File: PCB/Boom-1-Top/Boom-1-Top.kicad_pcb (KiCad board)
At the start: 4 copper layers, 345 x 165 mm, 770 parts, among them J1 DEBUG, J10 PIC_DEBUG, J11 PIC_DEBUG, J12 PIC_DEBUG, J13 PIC_DEBUG, J14 PIC_DEBUG, J15 USB_B_Micro, J16 SD_Card, J17 BT_DEBUG, J18 12V Supply, J19 3V3 Bypass, J2 MIDI IN, J20 5V Bypass, J3 MIDI OUT, J37 Osc1Conn, J38 Osc2Conn, J39 SubNoiseConn, J4 PIC_DEBUG, J40 FiltConn2, J41 EnvGenConn2, J42 EnvGenConn1, J43 FXConn1, J44 FiltConn1, J45 FXConn2, J46 EnvGenConn3, J5 PIC_DEBUG, J6 PIC_DEBUG, J7 PIC_DEBUG, J8 PIC_DEBUG, J9 PIC_DEBUG, Q1 AO3401A, Q2 AO3401A, SW1 Osc1SawEncoder, SW10 SubToOsc2FiltEncoder, SW11 Osc1ToOsc2FiltEncoder, SW12 Osc1FiltFreqEncoder, SW13 Osc2FiltFreqEncoder, SW14 SubFiltFreqEncoder, SW15 OscFiltEnvAttackEncoder, SW16 SubFiltEnvAttackEncoder, SW17 Osc1FiltResEncoder, SW18 Osc2FiltResEncoder, SW19 SubFiltResEncoder, SW2 Osc1SqrEncoder, SW20 OscFiltEnvDecayEncoder, SW21 SubFiltEnvDecayEncoder, SW22 OscFiltEnvSustainEncoder, SW23 SubFiltEnvSustainEncoder, SW24 Osc1DriveEncoder, SW25 Osc2DistortionEncoder, SW26 OscFiltEnvReleaseEncoder, SW27 SubFiltEnvReleaseEncoder, SW28 FXWetDryEncoder, SW29 SubAmpEnvAttackEncoder, SW3 Rotary_Encoder, SW30 OscAmpEnvAttackEncoder, SW31 FXControl1Encoder, SW32 SubAmpEnvDecayEncoder, SW33 OscAmpEnvDecayEncoder, SW34 FXControl2Encoder, SW35 SubAmpEnvSustainEncoder, SW36 OscAmpEnvSustainEncoder, SW37 FXControl3Encoder, SW38 FXFeedbackEncoder, SW39 SubAmpEnvReleaseEncoder, SW4 Rotary_Encoder_Switch, SW40 OscAmpEnvReleaseEncoder, SW41 Reset, SW43 Reset, SW5 Rotary_Encoder, SW53 Osc1TuneEncoder, SW6 SubToSubFiltEncoder, SW7 SubNoiseEncoder, U1 STM32F407VGTx, U10 DAC7678xPW, U11 PIC18F26Q43, U12 PIC18F26Q43, U13 PIC18F26Q43, U14 PIC18F26Q43, U15 PIC18F26Q43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

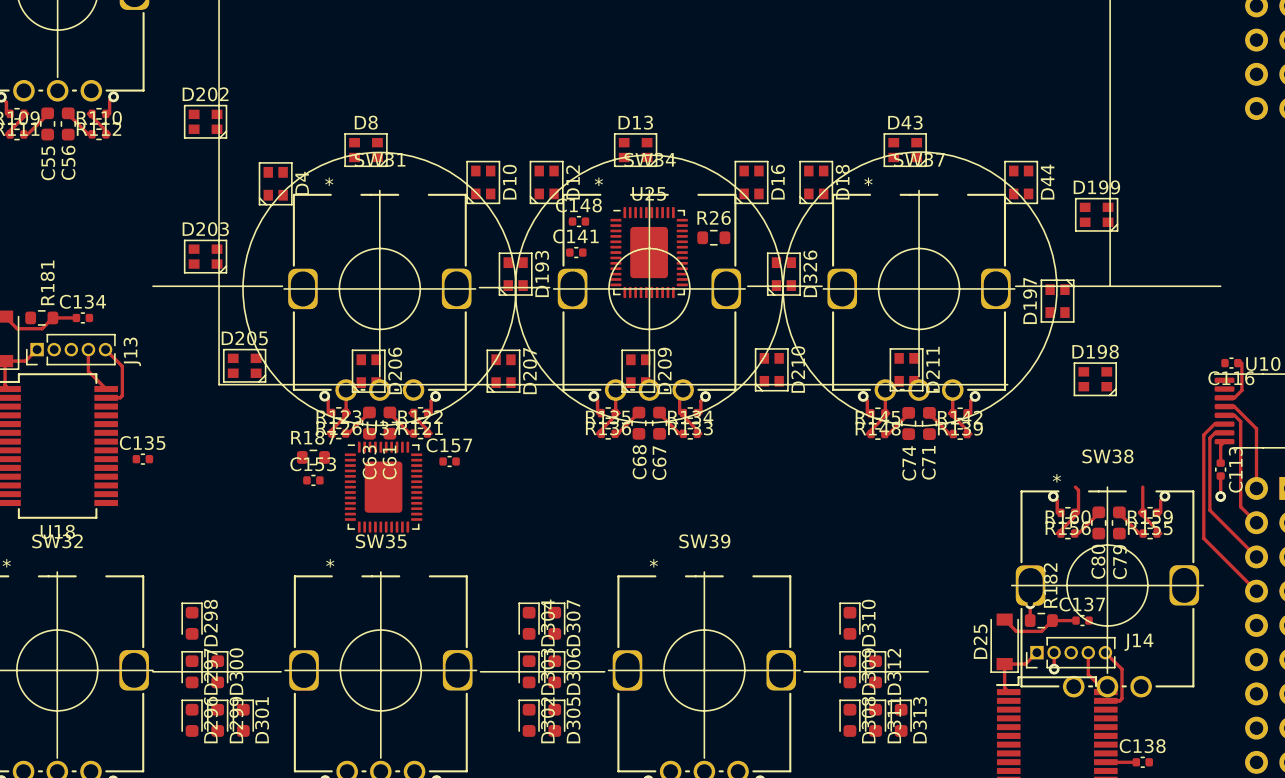
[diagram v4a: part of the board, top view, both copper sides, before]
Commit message: FX knobs in a row including feedback
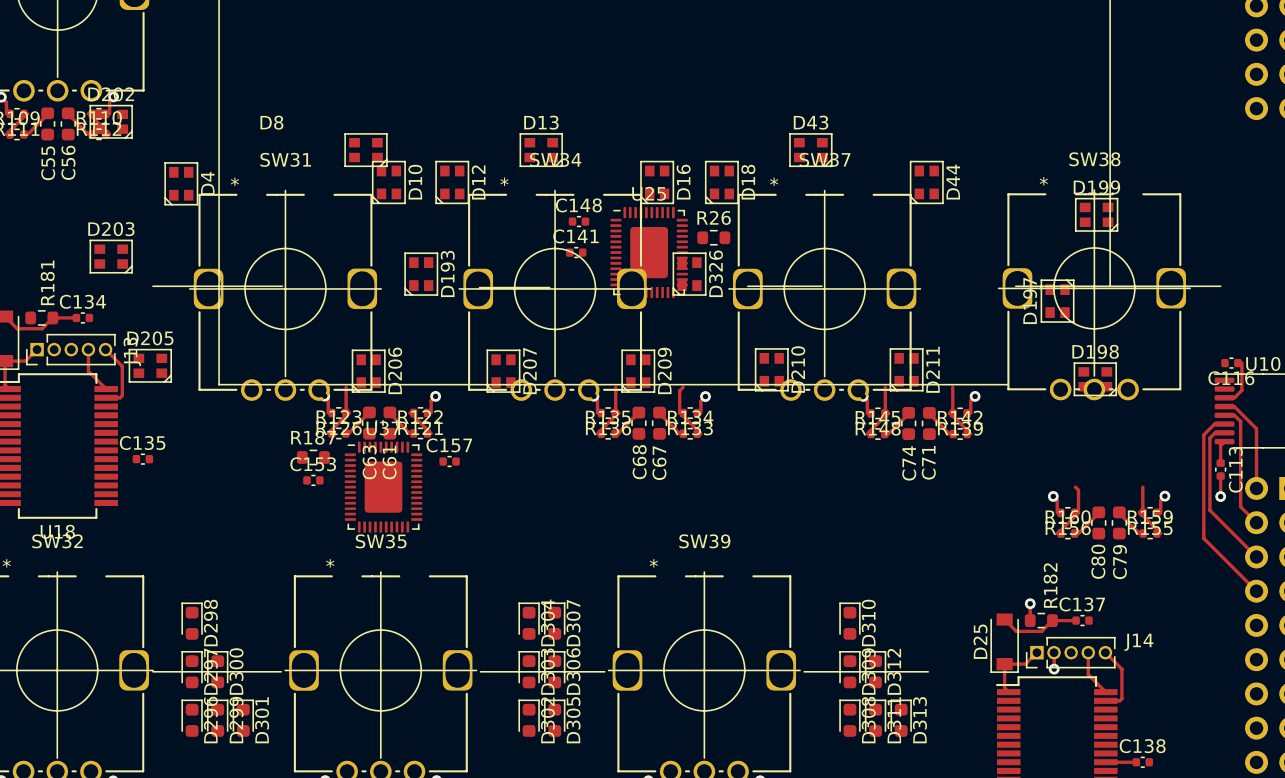
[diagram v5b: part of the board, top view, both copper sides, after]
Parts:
- moved SW38 22.1 mm to (454.9, 202.4)
- moved D10 7.00 mm to (405.1, 201.5)
- moved D12 7.00 mm to (409.8, 201.5)
- moved D13 7.00 mm to (416.4, 199.1)
- moved D16 7.00 mm to (425.0, 201.5)
- moved D18 7.00 mm to (429.8, 201.5)
- moved D193 7.00 mm to (407.5, 208.3)
- moved D202 7.00 mm to (384.5, 197.0)
- moved D203 7.00 mm to (384.5, 207.0)
- moved D205 7.00 mm to (387.4, 215.1)
- moved D326 7.00 mm to (427.4, 208.3)
- moved D4 7.00 mm to (389.7, 201.6)
- moved D43 7.00 mm to (436.4, 199.1)
- moved D44 7.00 mm to (445.0, 201.5)
- moved SW31 7.00 mm to (394.9, 202.4)
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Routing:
- net +5V: track 129.7 -> 125.6 mm, vias 81 -> 78
- net Net-(R139-Pad2): track 4.24 -> 5.62 mm, vias 0 -> 1
- net Net-(R133-Pad2): track 4.23 -> 5.59 mm, vias 0 -> 1
- net Net-(R121-Pad2): track 2.20 -> 3.56 mm, vias 0 -> 1
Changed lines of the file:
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@@
   (general
     (thickness 1.6)
-    (drawings 93)
+    (drawings 90)
     (tracks 1239)
     (zones 0)
@@
   )
   (module PEC11R:PEC11R-4x15F-N0024 locked (layer F.Cu)
-    (at 455.9 224.4)
+    (at 454.93 202.36)
     (fp_text reference SW38 (at 2.54 -2.54) (layer F.SilkS)
       (effects (font (size 1 1) (thickness 0.15)))
@@
   )
   (module PEC11R:PEC11R-4x15F-N0024 locked (layer F.Cu)
-    (at 441.925 202.4)
+    (at 434.925 202.4)
     (fp_text reference SW37 (at 2.54 -2.54) (layer F.SilkS)
       (effects (font (size 1 1) (thickness 0.15)))
@@
   )
   (module PEC11R:PEC11R-4x15F-N0024 locked (layer F.Cu)
-    (at 421.925 202.4)
+    (at 414.925 202.4)
     (fp_text reference SW34 (at 2.54 -2.54) (layer F.SilkS)
       (effects (font (size 1 1) (thickness 0.15)))
@@
   )
   (module PEC11R:PEC11R-4x15F-N0024 locked (layer F.Cu)
-    (at 401.925 202.4)
+    (at 394.925 202.4)
     (fp_text reference SW31 (at 2.54 -2.54) (layer F.SilkS)
       (effects (font (size 1 1) (thickness 0.15)))
@@
   )
   (module fm-b2020rgba-hg:FM-B2020RGBA-HG (layer F.Cu)
-    (at 434.4 208.3 270)
+    (at 427.4 208.3 270)
     (attr smd)
     (fp_text reference D326 (at 0 -2 90) (layer F.SilkS)
@@
   )
   (module fm-b2020rgba-hg:FM-B2020RGBA-HG (layer F.Cu)
-    (at 394.4 215.1)
+    (at 387.4 215.1)
     (attr smd)
     (fp_text reference D205 (at 0 -2) (layer F.SilkS)
@@
   )
   (module fm-b2020rgba-hg:FM-B2020RGBA-HG (layer F.Cu)
-    (at 391.5 207)
+    (at 384.5 207)
     (attr smd)
     (fp_text reference D203 (at 0 -2) (layer F.SilkS)
@@
   )
   (module fm-b2020rgba-hg:FM-B2020RGBA-HG (layer F.Cu)
-    (at 391.5 197)
+    (at 384.5 197)
     (attr smd)
     (fp_text reference D202 (at 0 -2) (layer F.SilkS)
@@
   )
   (module fm-b2020rgba-hg:FM-B2020RGBA-HG (layer F.Cu)
-    (at 414.5 208.3 270)
+    (at 407.5 208.3 270)
     (attr smd)
     (fp_text reference D193 (at 0 -2 90) (layer F.SilkS)
@@
   )
   (module fm-b2020rgba-hg:FM-B2020RGBA-HG (layer F.Cu)
-    (at 452 201.5 270)
+    (at 445 201.5 270)
     (attr smd)
     (fp_text reference D44 (at 0 -2 90) (layer F.SilkS)
@@
   )
   (module fm-b2020rgba-hg:FM-B2020RGBA-HG (layer F.Cu)
-    (at 443.4 199.1)
+    (at 436.4 199.1)
     (attr smd)
     (fp_text reference D43 (at 0 -2) (layer F.SilkS)
@@
   )
   (module fm-b2020rgba-hg:FM-B2020RGBA-HG (layer F.Cu)
-    (at 436.8 201.5 270)
+    (at 429.8 201.5 270)
     (attr smd)
     (fp_text reference D18 (at 0 -2 90) (layer F.SilkS)
@@
   )
   (module fm-b2020rgba-hg:FM-B2020RGBA-HG (layer F.Cu)
-    (at 432 201.5 270)
+    (at 425 201.5 270)
     (attr smd)
     (fp_text reference D16 (at 0 -2 90) (layer F.SilkS)
@@
   )
   (module fm-b2020rgba-hg:FM-B2020RGBA-HG (layer F.Cu)
-    (at 423.4 199.1)
+    (at 416.4 199.1)
     (attr smd)
     (fp_text reference D13 (at 0 -2) (layer F.SilkS)
@@
   )
   (module fm-b2020rgba-hg:FM-B2020RGBA-HG (layer F.Cu)
-    (at 416.8 201.5 270)
+    (at 409.8 201.5 270)
     (attr smd)
     (fp_text reference D12 (at 0 -2 90) (layer F.SilkS)
@@
   )
   (module fm-b2020rgba-hg:FM-B2020RGBA-HG (layer F.Cu)
-    (at 412.1 201.5 270)
+    (at 405.1 201.5 270)
     (attr smd)
     (fp_text reference D10 (at 0 -2 90) (layer F.SilkS)
@@
     (at 403.4 199.1)
     (attr smd)
-    (fp_text reference D8 (at 0 -2) (layer F.SilkS)
+    (fp_text reference D8 (at -7 -2) (layer F.SilkS)
       (effects (font (size 1 1) (thickness 0.15)))
     )
@@
   )
   (module fm-b2020rgba-hg:FM-B2020RGBA-HG (layer F.Cu)
-    (at 396.7 201.6 270)
+    (at 389.7 201.6 270)
     (attr smd)
     (fp_text reference D4 (at 0 -2 90) (layer F.SilkS)
@@
     (arrow2b (pts (xy 160.7 114.2) (xy 161.286421 115.326504)))
   )
-  (gr_circle (center 444.5 209.4) (end 436.7 202.9) (layer F.SilkS) (width 0.12))
-  (gr_circle (center 424.4 209.4) (end 416.9 202.9) (layer F.SilkS) (width 0.12))
-  (gr_circle (center 404.4 209.4) (end 411.2 201.9) (layer F.SilkS) (width 0.12))
   (gr_line (start 435.9 237.8) (end 445.1 237.8) (layer F.SilkS) (width 0.12))
   (gr_line (start 327.8 156.8) (end 336.9 156.8) (layer F.SilkS) (width 0.12))
@@
   (segment (start 432.3175 246.2025) (end 432.64 245.88) (width 0.25) (layer F.Cu) (net 204))
   (segment (start 432.3175 247.12) (end 432.3175 246.2025) (width 0.25) (layer F.Cu) (net 204))
-  (via (at 400.335 217.35) (size 0.8) (drill 0.4) (layers F.Cu B.Cu) (net 204))
-  (segment (start 400.595 217.61) (end 400.335 217.35) (width 0.25) (layer F.Cu) (net 204))
-  (segment (start 400.595 218.6) (end 400.595 217.61) (width 0.25) (layer F.Cu) (net 204))
+  (via (at 400.335 217.35) (size 0.8) (drill 0.4) (layers F.Cu B.Cu) (net 247))
+  (segment (start 400.595 217.61) (end 400.335 217.35) (width 0.25) (layer F.Cu) (net 247))
+  (segment (start 400.595 218.6) (end 400.595 217.61) (width 0.25) (layer F.Cu) (net 247))
   (via (at 408.565 217.37) (size 0.8) (drill 0.4) (layers F.Cu B.Cu) (net 204))
   (segment (start 408.2325 217.7025) (end 408.565 217.37) (width 0.25) (layer F.Cu) (net 204))
   (segment (start 408.2325 218.6) (end 408.2325 217.7025) (width 0.25) (layer F.Cu) (net 204))
-  (segment (start 420.5775 217.6325) (end 420.305 217.36) (width 0.25) (layer F.Cu) (net 204))
-  (via (at 420.305 217.36) (size 0.8) (drill 0.4) (layers F.Cu B.Cu) (net 204))
-  (segment (start 420.5775 218.61) (end 420.5775 217.6325) (width 0.25) (layer F.Cu) (net 204))
+  (segment (start 420.5775 217.6325) (end 420.305 217.36) (width 0.25) (layer F.Cu) (net 253))
+  (via (at 420.305 217.36) (size 0.8) (drill 0.4) (layers F.Cu B.Cu) (net 253))
+  (segment (start 420.5775 218.61) (end 420.5775 217.6325) (width 0.25) (layer F.Cu) (net 253))
   (via (at 428.585 217.38) (size 0.8) (drill 0.4) (layers F.Cu B.Cu) (net 204))
   (segment (start 428.2425 217.7225) (end 428.585 217.38) (width 0.25) (layer F.Cu) (net 204))
   (segment (start 428.2425 218.61) (end 428.2425 217.7225) (width 0.25) (layer F.Cu) (net 204))
-  (via (at 440.285 217.37) (size 0.8) (drill 0.4) (layers F.Cu B.Cu) (net 204))
-  (segment (start 440.5875 217.6725) (end 440.285 217.37) (width 0.25) (layer F.Cu) (net 204))
-  (segment (start 440.5875 218.63) (end 440.5875 217.6725) (width 0.25) (layer F.Cu) (net 204))
+  (via (at 440.285 217.37) (size 0.8) (drill 0.4) (layers F.Cu B.Cu) (net 257))
+  (segment (start 440.5875 217.6725) (end 440.285 217.37) (width 0.25) (layer F.Cu) (net 257))
+  (segment (start 440.5875 218.63) (end 440.5875 217.6725) (width 0.25) (layer F.Cu) (net 257))
   (segment (start 448.2625 217.6925) (end 448.585 217.37) (width 0.25) (layer F.Cu) (net 204))
   (via (at 448.585 217.37) (size 0.8) (drill 0.4) (layers F.Cu B.Cu) (net 204))

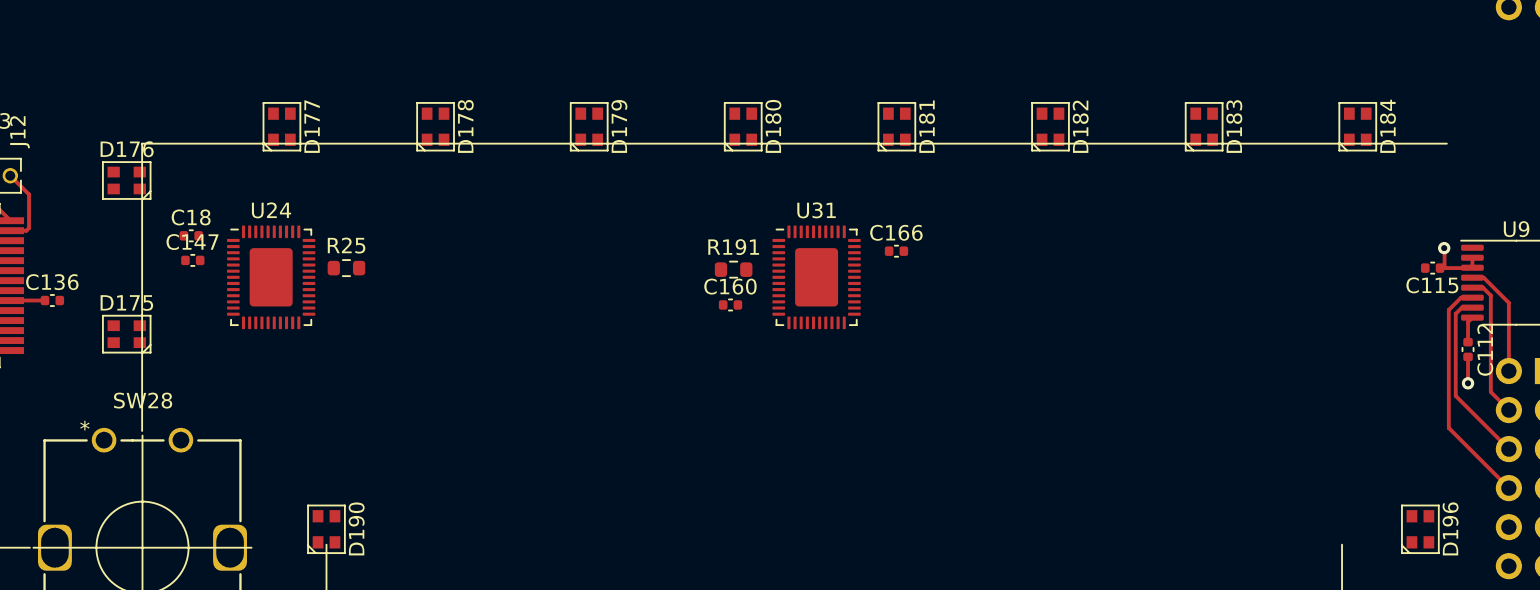
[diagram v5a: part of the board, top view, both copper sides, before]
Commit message: Horizontal guides are done and with new FX layout to accomodate a screen
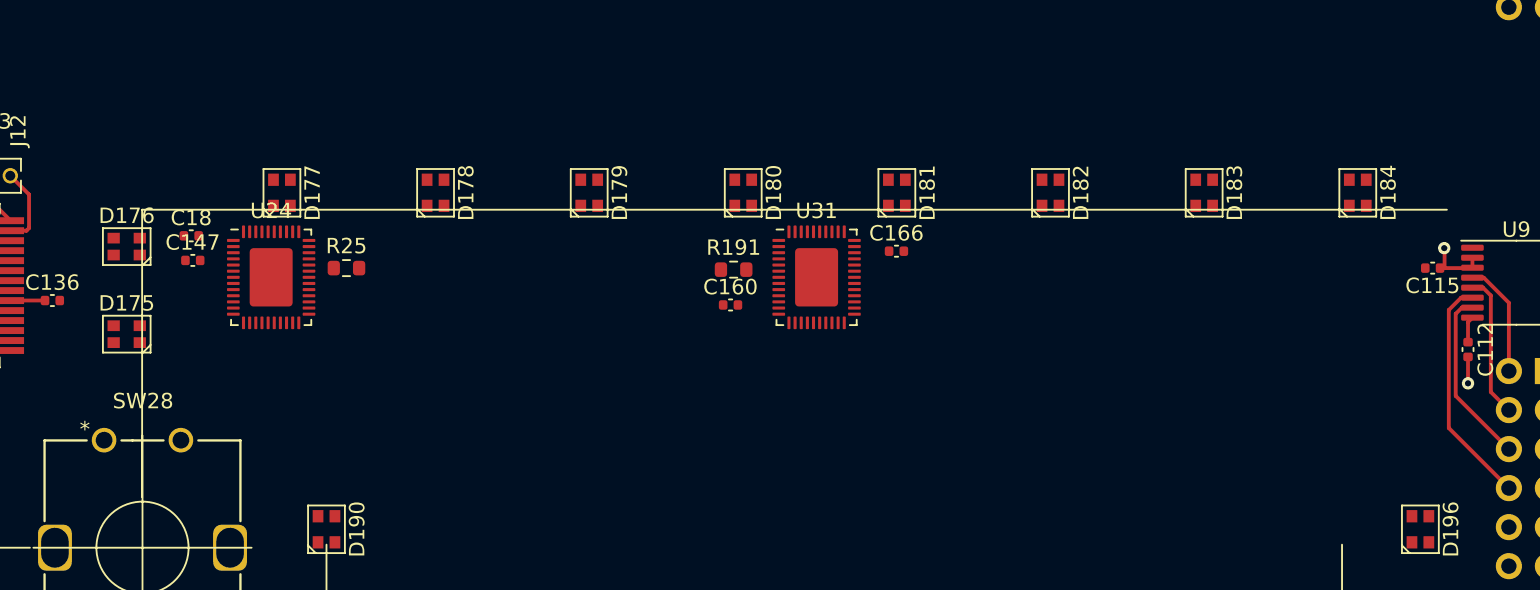
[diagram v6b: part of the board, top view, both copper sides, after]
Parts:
- moved D176 4.30 mm to (379.5, 167.6)
- moved D177 4.30 mm to (389.6, 164.1)
- moved D178 4.30 mm to (399.6, 164.1)
- moved D179 4.30 mm to (409.6, 164.1)
- moved D180 4.30 mm to (419.6, 164.1)
- moved D181 4.30 mm to (429.6, 164.1)
- moved D182 4.30 mm to (439.6, 164.1)
- moved D183 4.30 mm to (449.6, 164.1)
- moved D184 4.30 mm to (459.6, 164.1)
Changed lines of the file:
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@@
   (general
     (thickness 1.6)
-    (drawings 90)
+    (drawings 92)
     (tracks 1239)
     (zones 0)
@@
   )
   (module fm-b2020rgba-hg:FM-B2020RGBA-HG (layer F.Cu)
-    (at 459.625 159.8 270)
+    (at 459.625 164.1 270)
     (attr smd)
     (fp_text reference D184 (at 0 -2 90) (layer F.SilkS)
@@
   )
   (module fm-b2020rgba-hg:FM-B2020RGBA-HG (layer F.Cu)
-    (at 449.625 159.8 270)
+    (at 449.625 164.1 270)
     (attr smd)
     (fp_text reference D183 (at 0 -2 90) (layer F.SilkS)
@@
   )
   (module fm-b2020rgba-hg:FM-B2020RGBA-HG (layer F.Cu)
-    (at 439.625 159.8 270)
+    (at 439.625 164.1 270)
     (attr smd)
     (fp_text reference D182 (at 0 -2 90) (layer F.SilkS)
@@
   )
   (module fm-b2020rgba-hg:FM-B2020RGBA-HG (layer F.Cu)
-    (at 429.625 159.8 270)
+    (at 429.625 164.1 270)
     (attr smd)
     (fp_text reference D181 (at 0 -2 90) (layer F.SilkS)
@@
   )
   (module fm-b2020rgba-hg:FM-B2020RGBA-HG (layer F.Cu)
-    (at 419.625 159.8 270)
+    (at 419.625 164.1 270)
     (attr smd)
     (fp_text reference D180 (at 0 -2 90) (layer F.SilkS)
@@
   )
   (module fm-b2020rgba-hg:FM-B2020RGBA-HG (layer F.Cu)
-    (at 409.6 159.8 270)
+    (at 409.6 164.1 270)
     (attr smd)
     (fp_text reference D179 (at 0 -2 90) (layer F.SilkS)
@@
   )
   (module fm-b2020rgba-hg:FM-B2020RGBA-HG (layer F.Cu)
-    (at 399.6 159.8 270)
+    (at 399.6 164.1 270)
     (attr smd)
     (fp_text reference D178 (at 0 -2 90) (layer F.SilkS)
@@
   )
   (module fm-b2020rgba-hg:FM-B2020RGBA-HG (layer F.Cu)
-    (at 389.6 159.8 270)
+    (at 389.6 164.1 270)
     (attr smd)
     (fp_text reference D177 (at 0 -2 90) (layer F.SilkS)
@@
   )
   (module fm-b2020rgba-hg:FM-B2020RGBA-HG (layer F.Cu)
-    (at 379.5 163.3)
+    (at 379.5 167.6)
     (attr smd)
     (fp_text reference D176 (at 0 -2) (layer F.SilkS)
@@
     )
   )
-  (dimension 29 (width 0.15) (layer Dwgs.User)
-    (gr_text "29.000 mm" (at 449.5 201.7 270) (layer Dwgs.User)
+  (gr_line (start 388.7 209.2) (end 475.2 209.2) (layer Dwgs.User) (width 0.15))
+  (gr_line (start 390 165.2) (end 476.5 165.2) (layer Dwgs.User) (width 0.15))
+  (dimension 22 (width 0.15) (layer Dwgs.User)
+    (gr_text "22.000 mm" (at 442.3 176.2 90) (layer Dwgs.User)
       (effects (font (size 1 1) (thickness 0.15)))
     )
-    (feature1 (pts (xy 444.6 216.2) (xy 448.786421 216.2)))
-    (feature2 (pts (xy 444.6 187.2) (xy 448.786421 187.2)))
-    (crossbar (pts (xy 448.2 187.2) (xy 448.2 216.2)))
-    (arrow1a (pts (xy 448.2 216.2) (xy 447.613579 215.073496)))
-    (arrow1b (pts (xy 448.2 216.2) (xy 448.786421 215.073496)))
-    (arrow2a (pts (xy 448.2 187.2) (xy 447.613579 188.326504)))
-    (arrow2b (pts (xy 448.2 187.2) (xy 448.786421 188.326504)))
+    (feature1 (pts (xy 466.5 165.2) (xy 443.013579 165.2)))
+    (feature2 (pts (xy 466.5 187.2) (xy 443.013579 187.2)))
+    (crossbar (pts (xy 443.6 187.2) (xy 443.6 165.2)))
+    (arrow1a (pts (xy 443.6 165.2) (xy 444.186421 166.326504)))
+    (arrow1b (pts (xy 443.6 165.2) (xy 443.013579 166.326504)))
+    (arrow2a (pts (xy 443.6 187.2) (xy 444.186421 186.073496)))
+    (arrow2b (pts (xy 443.6 187.2) (xy 443.013579 186.073496)))
   )
   (dimension 22 (width 0.15) (layer Dwgs.User)
@@
   (gr_line (start 387.6 209.2) (end 397.2 209.2) (layer F.SilkS) (width 0.12))
   (gr_line (start 356.6 187.2) (end 373.2 187.2) (layer F.SilkS) (width 0.12))
-  (gr_line (start 380.5 179.6) (end 380.5 160.9) (layer F.SilkS) (width 0.12))
+  (gr_line (start 380.5 183.9) (end 380.5 165.2) (layer F.SilkS) (width 0.12))
   (gr_line (start 392.5 216.5) (end 392.5 187) (layer F.SilkS) (width 0.12))
   (gr_line (start 451 216.5) (end 392.5 216.5) (layer F.SilkS) (width 0.12))
@@
   (gr_line (start 364.1 136.7) (end 373.3 136.7) (layer F.SilkS) (width 0.12))
   (gr_line (start 314.9 126.3) (end 339.6 126.3) (layer F.SilkS) (width 0.12))
-  (gr_line (start 380.5 160.9) (end 465.425 160.9) (layer F.SilkS) (width 0.12))
+  (gr_line (start 380.5 165.2) (end 465.425 165.2) (layer F.SilkS) (width 0.12))
   (gr_line (start 431.725 209.2) (end 437.225 209.2) (layer F.SilkS) (width 0.12))
   (gr_line (start 411.825 209.3) (end 417.025 209.3) (layer F.SilkS) (width 0.12))
